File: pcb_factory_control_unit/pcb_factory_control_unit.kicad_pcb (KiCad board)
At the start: 4 copper layers, 188 x 65 mm, 275 parts, among them J1 STDC14, J17 STEP1, J18 STEP2, J2 Micro_SD_Card_Det1, J23 Weight, J3 INB, J30 Valve, J4 DC IN, J5 USB STM32, J6 USB STM32, Q1 IRLML6344, Q2 IRLML6344, Q3 IRLML6344, Q4 MMBT4403, Q5 IRLML6344, Q6 IRLML6344, SW1 Reset, SW2 Boot, U1 STM32H563VITx, U10 SIT3051TK, U11 74AHCT125, U12 TPS54202DDC, U16 24LC512, U2 LAN8742A, U4 TPS54202DDC, U5 AMS1117-3.3, U6 INA226, U7 TMC2209, U8 TMC2209, U9 HX711, X1 MT3608, Y1 25MHz, Y2 25MHz

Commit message: Minor changes
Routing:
- net Net-(U1-PE0): track 2.08 -> 52.3 mm
- net GND: track 843.2 -> 806.2 mm, vias 474 -> 471
- net +3V3: track 524.4 -> 523.4 mm
- net Net-(C11-Pad1): track 26.4 -> 27.4 mm
- net I2C1_SCL: track 93.6 -> 94.5 mm

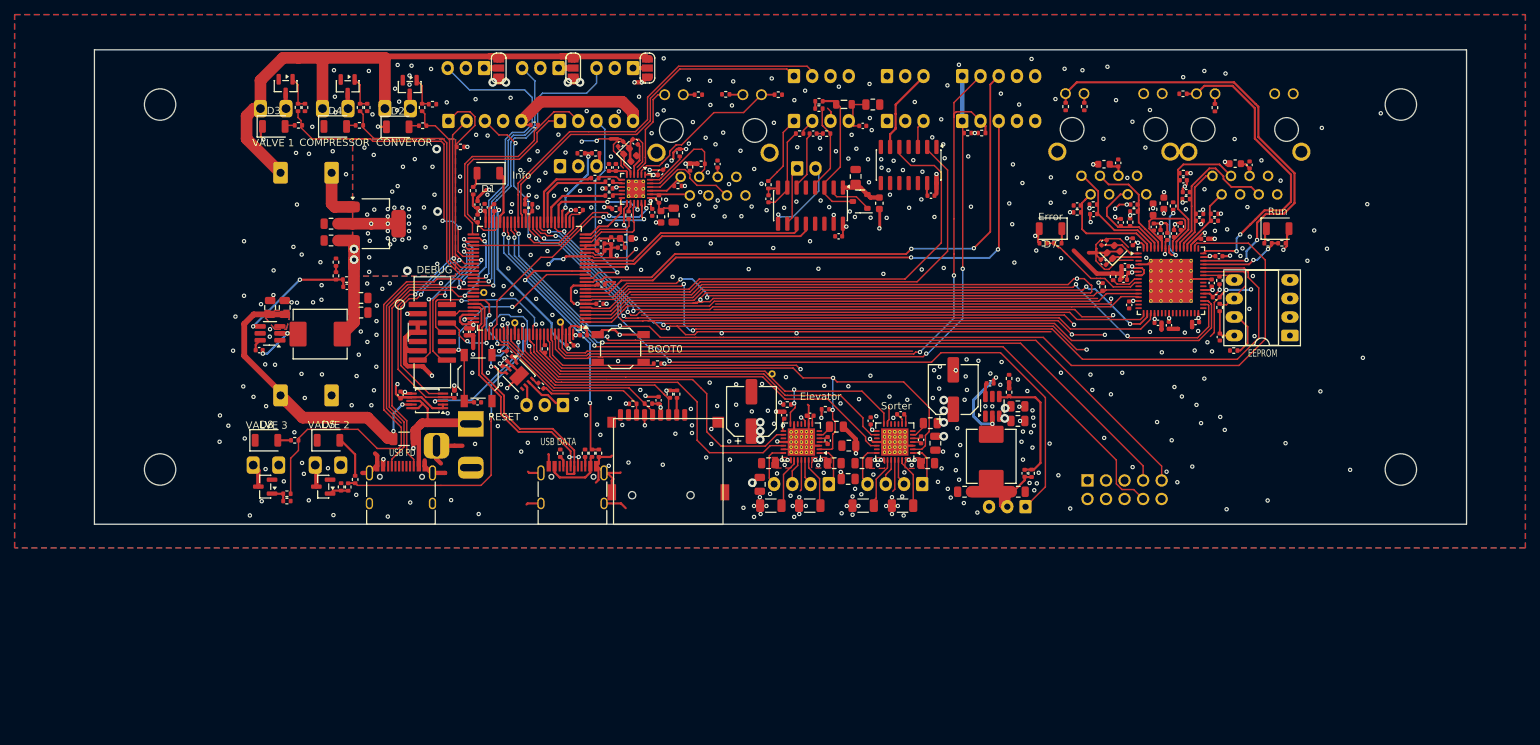
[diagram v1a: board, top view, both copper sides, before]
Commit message: Control Unit PCB: schematic rework (PSU, MX26631DL, XL6009 module, ERC fixes), new placement on 90 mm high board
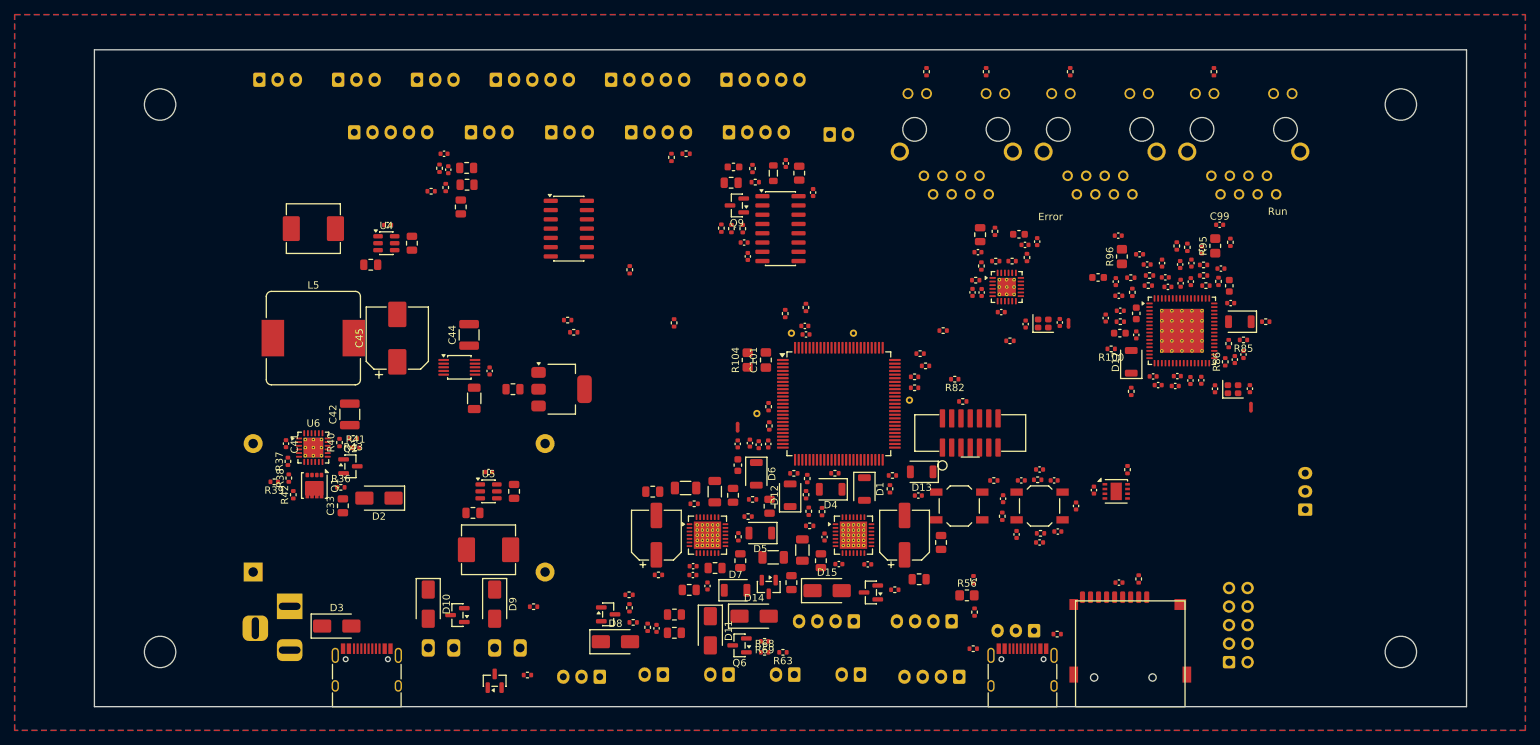
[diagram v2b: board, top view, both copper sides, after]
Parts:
- removed the C73 at (214.3, 73.3)
- removed the C85 at (210.2, 96.8)
- removed CanBus1: CAN, liebler_CONN:JST_XH_B3B-XH-A_1x03_P2.50mm_Vertical_smaller
- removed J30, Valve1, Valve2: Valve, liebler_CONN:PhoenixContact_MC_1,5_2-G-3.5_1x02_P3.50mm_Horizontal_smallerCourtyard
- removed JP1, JP2, JP3: 5-24, Jumper:SolderJumper-3_P1.3mm_Open_RoundedPad1.0x1.5mm_NumberLabels
- removed LB3: LightBarrier3, liebler_CONN:JST_XH_B3B-XH-A_1x03_P2.50mm_Vertical_smaller
- removed the R80 at (186.0, 84.0)
- removed the R83 at (210.1, 89.1)
- removed the R84 at (210.2, 92.8)
- removed U16: 24LC512, Package_DIP:DIP-8_W7.62mm_Socket_LongPads
- removed UEXT1: BH10S, ayluna:UEXTM-PTH
- added C101: 4n7/2k, Capacitor_SMD:C_0805_2012Metric_Pad1.18x1.45mm_HandSolder, F.Cu at (148.0, 100.0)
- added C33: 1u/50V, Capacitor_SMD:C_0805_2012Metric, F.Cu at (90.0, 120.0)
- added C41: u1/16V, Capacitor_SMD:C_0402_1005Metric, F.Cu at (82.2, 111.5)
- added C42: 10u/50V, Capacitor_SMD:C_1210_3225Metric, F.Cu at (91.0, 107.5)
- added C44: 10u/50V, Capacitor_SMD:C_1210_3225Metric, F.Cu at (107.3, 96.6)
- added C45: 100u/50V, Capacitor_SMD:CP_Elec_8x10, F.Cu at (97.5, 97.0)
- added C99: 22n/50V, Capacitor_SMD:C_0402_1005Metric, F.Cu at (210.2, 81.5)
- added D10: SS34, Diode_SMD:D_SMA, F.Cu at (101.7, 133.4)
- added D11: SS34, Diode_SMD:D_SMA, F.Cu at (140.4, 137.1)
- added D14: SS34, Diode_SMD:D_SMA, F.Cu at (146.4, 135.1)
- added D15: SS34, Diode_SMD:D_SMA, F.Cu at (156.4, 131.6)
- added D2: SMBJ24CA, Diode_SMD:D_SMA, F.Cu at (95.0, 118.9)
- added D3: SMAJ22CA, Diode_SMD:D_SMA, F.Cu at (89.2, 136.5)
- added D7: Vacuum Valve, LED_SMD:LED_1206_3216Metric_ReverseMount_Hole1.8x2.4mm, F.Cu at (143.8, 131.6)
- added D8: SS34, Diode_SMD:D_SMA, F.Cu at (127.4, 138.6)
- added D9: SS34, Diode_SMD:D_SMA, F.Cu at (110.8, 133.4)
- added J1: CAN, liebler_CONN:JST_XH_B3B-XH-A_1x03_P2.50mm_Vertical_smaller, B.Cu at (221.9, 118.0)
- added J15: UEXT, Connector_IDC:IDC-Header_2x05_P2.54mm_Vertical, B.Cu at (211.5, 141.4)
- added J19: Vacuum Pump, liebler_CONN:JST_XH_B3B-XH-A_1x03_P2.50mm_Vertical_smaller, B.Cu at (122.7, 143.4)
- added J21: Cylinder Valve, Connector_JST:JST_XH_B2B-XH-A_1x02_P2.50mm_Vertical, B.Cu at (133.9, 143.1)
- added J22: RoArm, liebler_CONN:JST_XH_B4B-XH-A_1x04_P2.50mm_Vertical_smaller, B.Cu at (170.7, 143.4)
- added J25: Vacuum Valve, Connector_JST:JST_XH_B2B-XH-A_1x02_P2.50mm_Vertical, B.Cu at (142.9, 143.1)
- added J26: Disturbance1, Connector_JST:JST_XH_B2B-XH-A_1x02_P2.50mm_Vertical, B.Cu at (151.9, 143.1)
- added J27: Disturbance2, Connector_JST:JST_XH_B2B-XH-A_1x02_P2.50mm_Vertical, B.Cu at (160.9, 143.1)
- added L5: 4.7uH, Inductor_SMD:L_Bourns_SRP1245A, F.Cu at (86.0, 97.0)
- added Q1: 40N06D, Package_SON:VSON-8_3.3x3.3mm_P0.65mm_NexFET, F.Cu at (86.1, 117.2)
- added Q2: BSS138, Package_TO_SOT_SMD:SOT-23, F.Cu at (91.1, 114.6)
- added Q6: AO3400, Package_TO_SOT_SMD:SOT-23, F.Cu at (144.4, 139.1)
- added R100: 3k3, Resistor_SMD:R_0402_1005Metric, F.Cu at (195.3, 98.5)
- added R104: 0, Resistor_SMD:R_0805_2012Metric_Pad1.20x1.40mm_HandSolder, F.Cu at (145.5, 100.0)
- added R36: 330k, Resistor_SMD:R_0402_1005Metric, F.Cu at (89.8, 117.5)
- added R37: 6k8, Resistor_SMD:R_0402_1005Metric, F.Cu at (82.5, 113.9)
- added R38: 15k, Resistor_SMD:R_0402_1005Metric, F.Cu at (82.6, 116.2)
- added R39: 1k, Resistor_SMD:R_0402_1005Metric, F.Cu at (80.6, 116.7)
- added R40: 330k, Resistor_SMD:R_0402_1005Metric, F.Cu at (89.6, 111.3)
- added R41: 22k, Resistor_SMD:R_0402_1005Metric, F.Cu at (91.8, 112.0)
- added R42: 10k, Resistor_SMD:R_0402_1005Metric, F.Cu at (83.2, 118.5)
- added R43: 10k, Resistor_SMD:R_0402_1005Metric, F.Cu at (91.5, 110.8)
- added R63: 1k, Resistor_SMD:R_0402_1005Metric, F.Cu at (150.3, 140.1)
- added R68: 1k, Resistor_SMD:R_0402_1005Metric, F.Cu at (147.8, 140.1)
- added R69: 10k, Resistor_SMD:R_0402_1005Metric, F.Cu at (147.8, 138.6)
- added R82: 10k, Resistor_SMD:R_0402_1005Metric, F.Cu at (173.9, 102.6)
- added R86: 3k3, Resistor_SMD:R_0402_1005Metric, F.Cu at (210.9, 100.2)
- added R95: 0, Resistor_SMD:R_0805_2012Metric_Pad1.20x1.40mm_HandSolder, F.Cu at (209.6, 84.4)
- added R96: 0, Resistor_SMD:R_0805_2012Metric_Pad1.20x1.40mm_HandSolder, F.Cu at (196.8, 85.8)
- added U6: MX26631DL, Package_DFN_QFN:Texas_RGE0024H_VQFN-24-1EP_4x4mm_P0.5mm_EP2.7x2.7mm_ThermalVias, F.Cu at (86.0, 112.0)
- D12: renamed from D5; value Valve -> Disturbance1
- D13: renamed from D8; value Valve -> Disturbance2
- D5: renamed from D2; value Motor -> Conveyor
- IJ1: renamed from I2C2; value TOF2 -> I2C2
- J17: value STEP1 -> Elevator
- J18: value STEP2 -> Sorter
- J7: renamed from I2C4; value TOF3 -> I2C4
- J8: renamed from I2C1B1; value TOF1 -> I2C1B
- J9: renamed from I2C1A1; value RGB -> I2C1A
- Q3: renamed from Q2; value IRLML6344 -> AO3400
- Q4: renamed from Q1; value IRLML6344 -> AO3400
- Q5: renamed from Q3; value IRLML6344 -> AO3400
- Q7: renamed from Q5; value IRLML6344 -> AO3400
- Q8: renamed from Q6; value IRLML6344 -> AO3400
- Q9: renamed from Q4; footprint liebler_SEMICONDUCTORS:SOT-23_smaller -> Package_TO_SOT_SMD:SOT-23
- R56: renamed from R52; footprint Resistor_SMD:R_0402_1005Metric -> Resistor_SMD:R_0805_2012Metric_Pad1.20x1.40mm_HandSolder
- R85: value 10k -> 3k3
- R98: renamed from R78; value 10k -> 3k3
- U4: footprint Package_TO_SOT_SMD:SOT-23-6_Handsoldering -> Package_TO_SOT_SMD:SOT-23-6
- U5: renamed from U12; footprint Package_TO_SOT_SMD:SOT-23-6_Handsoldering -> Package_TO_SOT_SMD:SOT-23-6
- X1: value MT3608 -> XL6009 (24V); footprint liebler_MODULES:DCDC_MT3608 -> liebler_MODULES:DCDC-XL6009-boost
- moved D4 91.1 mm to (156.9, 117.7), turned to 180 degrees
- moved D13 89.9 mm to (169.3, 115.3), turned to 180 degrees
- moved C7 88.8 mm to (185.5, 125.0), turned to 0 degrees
- moved R58 87.7 mm to (153.9, 120.7), turned to -90 degrees
- moved C8 86.0 mm to (190.5, 120.0), turned to 90 degrees
- moved Q3 84.8 mm to (126.4, 134.8), turned to 0 degrees
- moved Q8 84.2 mm to (162.4, 131.8)
- moved R75 84.2 mm to (165.7, 131.5)
- moved J9 83.7 mm to (96.6, 68.8)
- moved C11 83.5 mm to (183.0, 116.5), turned to 0 degrees
- moved R59 83.3 mm to (145.6, 121.5), turned to 0 degrees
- moved U2 83.3 mm to (196.0, 118.0), turned to 0 degrees
- moved C10 83.1 mm to (187.5, 116.5), turned to 0 degrees
- moved R74 82.6 mm to (165.0, 117.7), turned to 90 degrees
- moved C17 82.6 mm to (192.9, 117.8), turned to 90 degrees
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- renumbered C8 to C10, C58 to C100, C9 to C11, C10 to C12, C11 to C13, C12 to C14, C13 to C15, C61 to C17, C17 to C18, C18 to C19, C14 to C2, C19 to C20, C20 to C21, C21 to C22, C22 to C23, C23 to C24, C24 to C25, C75 to C26, C76 to C28, C28 to C29, C2 to C3, C80 to C30, C29 to C31, C84 to C32, C30 to C34, C88 to C35, C31 to C36, C89 to C37, C32 to C38, C98 to C39, C15 to C4, C33 to C40, C34 to C43, C35 to C46, C36 to C47, C37 to C48, C38 to C49, C3 to C5, C39 to C50, C40 to C51, C41 to C52, C42 to C53, C43 to C54, C44 to C55, C45 to C56, C46 to C57, C47 to C58, C48 to C59, C4 to C6, C49 to C60, C50 to C61, C51 to C62, C62 to C63, C52 to C64, C53 to C65, C54 to C66, C55 to C67, C56 to C68, C60 to C69, C5 to C7, C57 to C70, C59 to C71, C74 to C73, C77 to C74, C78 to C75, C83 to C76, C63 to C77, C68 to C78, C71 to C79, C6 to C8, C64 to C80, C79 to C81, C69 to C82, C65 to C83, C81 to C84, C86 to C85, C66 to C86, C82 to C87, C87 to C88, C67 to C89, C7 to C9, C70 to C90, C90 to C91, C94 to C92, C91 to C93, C95 to C94, C92 to C95, C93 to C97, C97 to C98, D6 to D16, D7 to D17, D3 to D4, D4 to D6, Leds1 to J10, Leds2 to J11, LB1 to J12, LB2 to J13, Pressure1 to J14, Malibotti1 to J16, J1 to J2, Robot1 to J20, Conv1 to J23, Comp1 to J24, J3 to J28, J23 to J29, J2 to J3, L7 to L10, L5 to L11, L10 to L4, L4 to L6, L6 to L7, NT4 to NT3, R10 to R1, R3 to R10, R81 to R101, R82 to R102, R66 to R103, R86 to R105, R62 to R13, R13 to R14, R63 to R15, R14 to R16, R16 to R17, R17 to R18, R18 to R19, R4 to R2, R76 to R21, R24 to R22, R25 to R23, R15 to R24, R26 to R25, R27 to R26, R28 to R27, R29 to R28, R30 to R29, R5 to R3, R31 to R30, R87 to R31, R88 to R34, R96 to R35, R6 to R4, R34 to R44, R35 to R45, R36 to R46, R37 to R47, R38 to R48, R40 to R49, R7 to R5, R39 to R50, R41 to R51, R42 to R52, R43 to R53, R44 to R54, R46 to R55, R54 to R57, R49 to R58, R50 to R59, R8 to R6, R51 to R60, R45 to R61, R53 to R62, R47 to R64, R48 to R65, R55 to R66, R56 to R67, R9 to R7, R90 to R70, R93 to R71, R91 to R72, R92 to R73, R94 to R74, R95 to R75, R57 to R76, R58 to R77, R59 to R78, R60 to R79, R1 to R8, R61 to R80, R64 to R81, R65 to R83, R67 to R84, R68 to R87, R72 to R88, R69 to R89, R2 to R9, R73 to R90, R70 to R91, R74 to R92, R71 to R93, R75 to R94, R77 to R97, R79 to R99, TP5 to TP1, TP4 to TP2, TP1 to TP4, U8 to U10, U9 to U12, U10 to U2, U2 to U3, U5 to U7, U6 to U8, U7 to U9
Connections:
- C100 pad 1: /EtherCAT/VDD33TXRX2 -> Net-(EthercatB1-RCT)
- C27 pad 2: 5-24V -> +24V
- C28 pad 2: 5-24V -> +24V
- C29 pad 2: 5-24V -> +24V
- C30 pad 2: 5-24V -> +24V
- C47 pad 1: 5-24V -> +24V
- C48 pad 1: 5-24V -> +24V
- C51 pad 1: 5-24V -> +24V
- C52 pad 1: 5-24V -> +24V
- C53 pad 1: 5-24V -> +24V
- C54 pad 1: 5-24V -> +24V
- C59 pad 2: 5-24V -> +24V
- C60 pad 2: 5-24V -> +24V
- C61 pad 2: 5-24V -> +24V
- C62 pad 2: 5-24V -> +24V
- C64 pad 1: 5-24V -> +24V
- C65 pad 1: 5-24V -> +24V
- D16 pad 2: +3V3 -> RUNLED
- D17 pad 2: +3V3 -> ERRLED
- EthercatA1 pad 4: /EtherCAT/VDD33TXRX1 -> Net-(EthercatA1-RCT)
- EthercatA1 pad 5: /EtherCAT/VDD33TXRX1 -> Net-(EthercatA1-RCT)
- EthercatA1 pad 8: GND -> GND1
- EthercatA1 pad SH: GND -> GND1
- EthercatB1 pad 4: /EtherCAT/VDD33TXRX2 -> Net-(EthercatB1-RCT)
- EthercatB1 pad 5: /EtherCAT/VDD33TXRX2 -> Net-(EthercatB1-RCT)
- EthercatB1 pad 8: GND -> GND1
- EthercatB1 pad SH: GND -> GND1
- J12 pad 1: Net-(JP2-C) -> +24V
- J13 pad 1: Net-(JP1-C) -> +24V
- J4 pad 1: +VDC -> Net-(D2-A2)
- J5 pad A4: +VDC -> Net-(D3-A2)
- J5 pad A9: +VDC -> Net-(D3-A2)
- J5 pad B4: +VDC -> Net-(D3-A2)
- J5 pad B9: +VDC -> Net-(D3-A2)
- R44 pad 2: 5-24V -> +24V
- R85 pad 1: Net-(U16-WP) -> +3V3
- R85 pad 2: GND -> Net-(U13A-EESCL)
- R97 pad 2: RUNLED -> GND
- R98 pad 1: +3V3 -> RUNLED
- R98 pad 2: RUNLED -> GND
- R99 pad 2: ERRLED -> GND
- U1 pad 65: LightBarrier3 -> unconnected-(U1-PC8-Pad65)
- U1 pad 79: unconnected-(U1-PC11-Pad79) -> VACUUM_PUMP
- U10 pad 22: 5-24V -> +24V
- U10 pad 28: 5-24V -> +24V
- U11 pad 8: unconnected-(U11-Pad8) -> Net-(J19-Pin_3)
- U11 pad 9: GND -> VACUUM_PUMP
- U13 pad 25: OE_EXT -> unconnected-(U13B-A1/ALELO/OE_EXT/MII_CLK25/EE_EMUL_SPI2-Pad25)
- U13 pad 42: EESDA -> Net-(U13A-EESDA)
- U13 pad 43: EESCL -> Net-(U13A-EESCL)
- U4 pad 3: 5-24V -> +24V
- U5 pad 3: 5-24V -> +24V
- U8 pad 9: 5-24V -> +24V
- U9 pad 22: 5-24V -> +24V
- U9 pad 28: 5-24V -> +24V
- X1 pad 1: 5-24V -> Net-(D3-A2)
- X1 pad 4: +24V -> Net-(D2-A2)
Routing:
- net GND: track 806.2 -> 0.00 mm, vias 471 -> 0
- net +3V3: track 523.4 -> 0.00 mm, vias 76 -> 0
- net 5-24V: track 200.3 -> 0.00 mm, vias 26 -> 0
- net +5V: track 170.1 -> 0.00 mm, vias 9 -> 0
- net +24V: track 154.5 -> 0.00 mm
- net QSPI_CS: track 136.9 -> 0.00 mm, vias 2 -> 0
- net ETHERCAT_IRQ: track 118.1 -> 0.00 mm, vias 2 -> 0
- net SPI4_MOSI: track 107.9 -> 0.00 mm, vias 2 -> 0
- net SPI4_CLK: track 107.6 -> 0.00 mm, vias 2 -> 0
- net SPI4_MISO: track 105.3 -> 0.00 mm, vias 2 -> 0
- net QSPI_SIO3: track 102.7 -> 0.00 mm, vias 2 -> 0
- net ROBOT_RX: track 102.4 -> 0.00 mm, vias 2 -> 0
- net I2C1_SDA: track 99.9 -> 0.00 mm, vias 2 -> 0
- net SYNC0: track 94.6 -> 0.00 mm, vias 2 -> 0
- net I2C1_SCL: track 94.5 -> 0.00 mm, vias 2 -> 0
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- removed copper zone on B.Cu, net +3V3
- removed copper zone on F.Cu, net +3V3
- removed copper zone on B.Cu, net 5-24V
- removed copper zone on F.Cu, net 5-24V
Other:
- board size 188 x 65 mm -> 188 x 90 mm
- board text added: "Niemals gleichzeitig USB-PD und DC-IN"

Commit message: Control Unit PCB: autorouted first pass (483/540 connections, GND via fanout to In1)
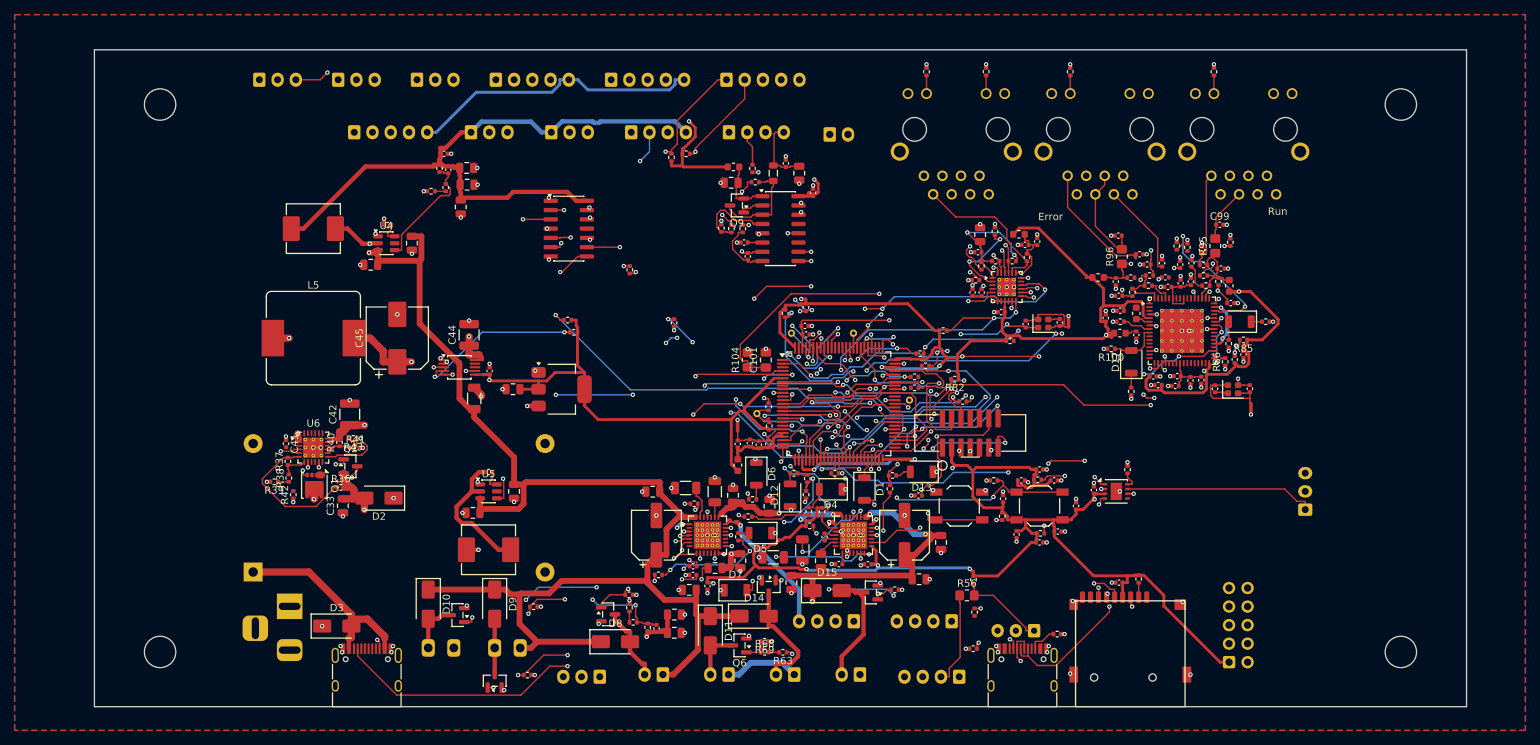
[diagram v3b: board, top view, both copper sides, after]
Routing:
- net +3V3: track 0.00 -> 648.3 mm, vias 0 -> 23
- net +24V: track 0.00 -> 359.9 mm, vias 0 -> 8
- net +5V: track 0.00 -> 141.7 mm, vias 0 -> 1
- net LightBarrier1: track 0.00 -> 127.2 mm, vias 0 -> 2
- net I2C4_SCL: track 0.00 -> 127.1 mm, vias 0 -> 3
- net I2C4_SDA: track 0.00 -> 120.1 mm, vias 0 -> 4
- net I2C1_SCL: track 0.00 -> 113.9 mm, vias 0 -> 3
- net LightBarrier2: track 0.00 -> 112.8 mm, vias 0 -> 1
- net USBPD_CC2: track 0.00 -> 111.8 mm, vias 0 -> 2
- net GND: track 0.00 -> 111.0 mm, vias 0 -> 208
- net +12V: track 0.00 -> 110.5 mm, vias 0 -> 2
- net I2C1_SDA: track 0.00 -> 108.3 mm, vias 0 -> 2
- net GND1: track 0.00 -> 108.1 mm, vias 0 -> 1
- net USBPD_CC1: track 0.00 -> 105.3 mm, vias 0 -> 9
- net INT_RGB: track 0.00 -> 102.9 mm, vias 0 -> 1
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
